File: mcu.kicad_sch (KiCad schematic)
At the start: 26 parts, among them J1 Debugger, J5 UART, J7 GPIO, SW1 BOOT, U1 STM32F103C8Tx, U2 SN65HVD230, Y1 8 Mhz 5032

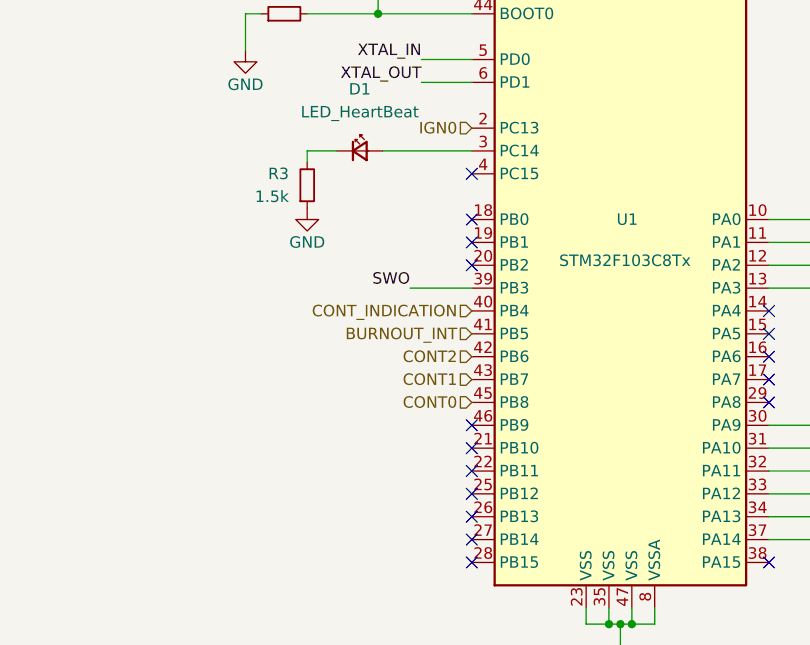
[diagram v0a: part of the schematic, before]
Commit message: Update ignition system with CDI
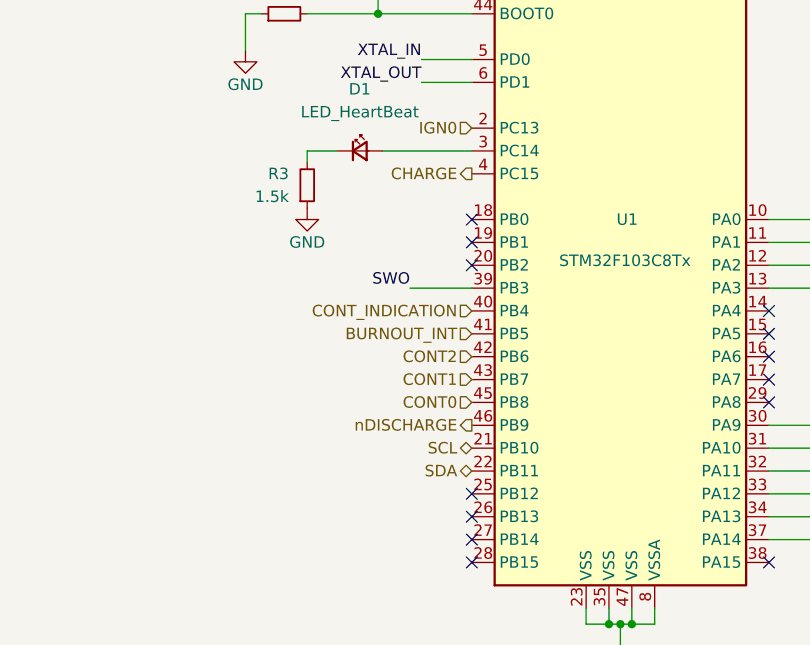
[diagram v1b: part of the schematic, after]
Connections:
- net SCL: now reaches U1.21 (PB10)
- net SDA: now reaches U1.22 (PB11)
- net CHARGE: now reaches U1.4 (PC15)
- net nDISCHARGE: now reaches U1.46 (PB9)
- no-connect marks 20 -> 16
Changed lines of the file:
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@@
   (junction (at 236.22 30.226) (diameter 0.9144) (color 0 0 0 0))
   (junction (at 236.22 38.862) (diameter 0.9144) (color 0 0 0 0))
-  (no_connect (at 74.676 97.028))
   (no_connect (at 74.676 102.108))
   (no_connect (at 74.676 104.648))
   (no_connect (at 74.676 107.188))
-  (no_connect (at 74.676 124.968))
-  (no_connect (at 74.676 127.508))
-  (no_connect (at 74.676 130.048))
   (no_connect (at 74.676 132.588))
   (no_connect (at 74.676 135.128))
@@
     (effects (font (size 1.27 1.27)) (justify right))
   )
+  (hierarchical_label "CHARGE" (shape output) (at 74.676 97.028 180)
+    (effects (font (size 1.27 1.27)) (justify right))
+  )
   (hierarchical_label "CONT_INDICATION" (shape input) (at 74.676 112.268 180)
     (effects (font (size 1.27 1.27)) (justify right))
@@
     (effects (font (size 1.27 1.27)) (justify right))
   )
+  (hierarchical_label "nDISCHARGE" (shape output) (at 74.676 124.968 180)
+    (effects (font (size 1.27 1.27)) (justify right))
+  )
+  (hierarchical_label "SCL" (shape bidirectional) (at 74.676 127.508 180)
+    (effects (font (size 1.27 1.27)) (justify right))
+  )
+  (hierarchical_label "SDA" (shape bidirectional) (at 74.676 130.048 180)
+    (effects (font (size 1.27 1.27)) (justify right))
+  )

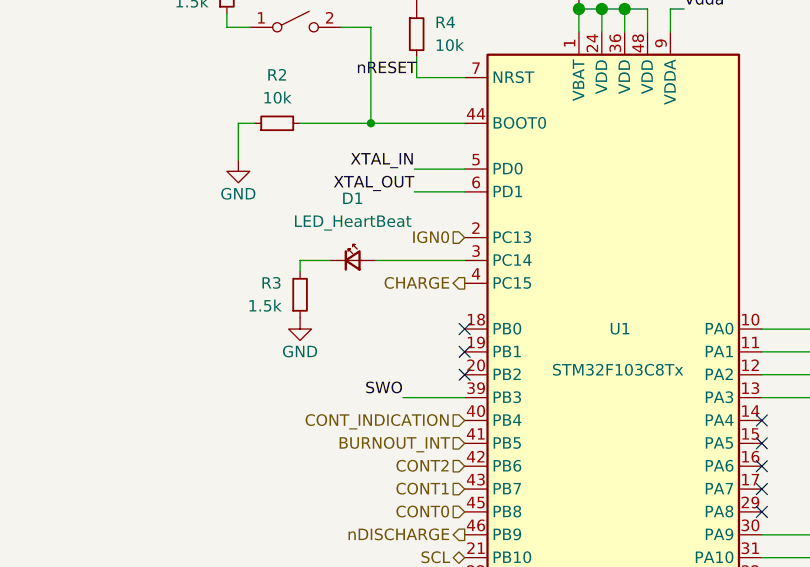
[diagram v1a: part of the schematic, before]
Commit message: #4 add pchannel for charge and nchannel for ignition
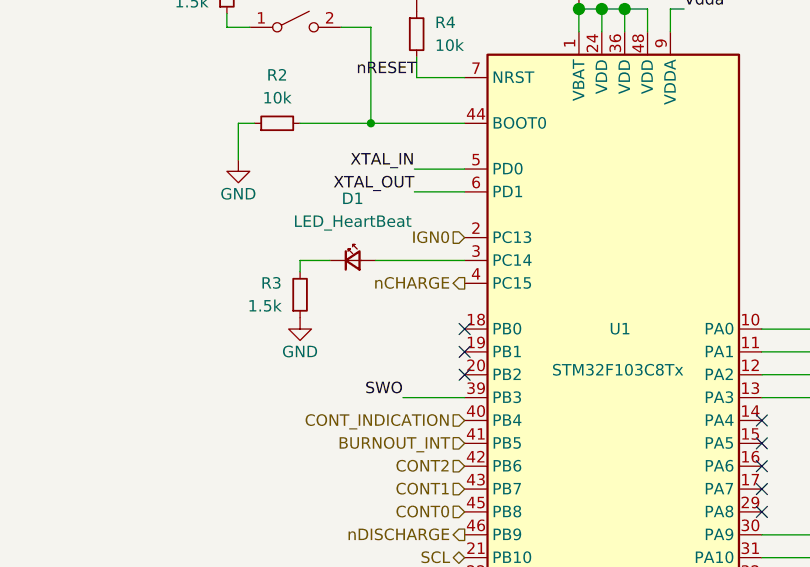
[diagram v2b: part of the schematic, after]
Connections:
- net CHARGE renamed nCHARGE
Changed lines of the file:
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@@
     (effects (font (size 1.27 1.27)) (justify right))
   )
-  (hierarchical_label "CHARGE" (shape output) (at 74.676 97.028 180)
+  (hierarchical_label "nCHARGE" (shape output) (at 74.676 97.028 180)
     (effects (font (size 1.27 1.27)) (justify right))
   )

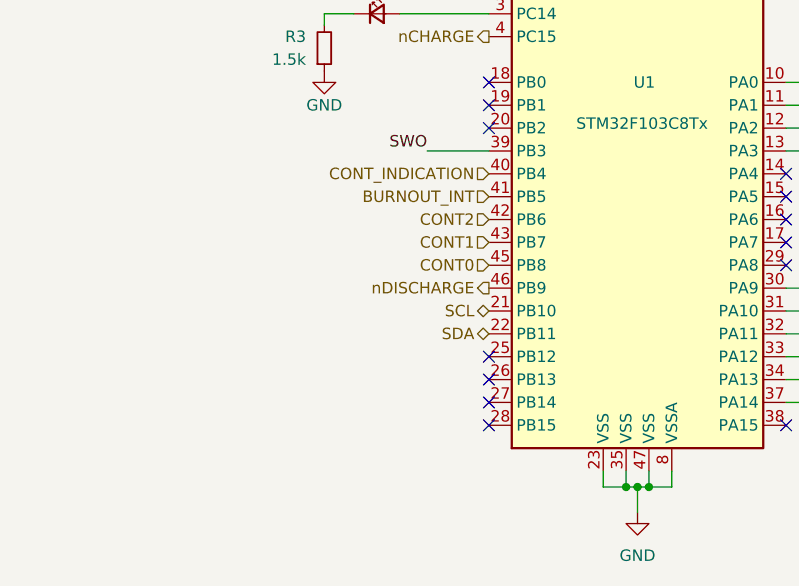
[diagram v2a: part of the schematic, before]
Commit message: #1 New pyro channel introduced in schematic
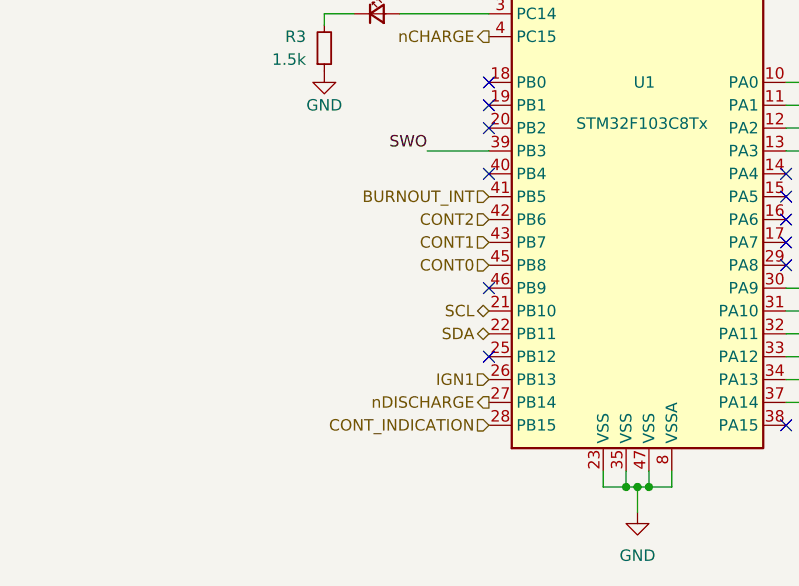
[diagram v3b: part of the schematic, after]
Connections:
- net CONT_INDICATION: now also U1.28 (PB15); no longer U1.40 (PB4)
- net nDISCHARGE: now also U1.27 (PB14); no longer U1.46 (PB9)
- net IGN1: now reaches U1.26 (PB13)
- no-connect marks 16 -> 15
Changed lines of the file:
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@@
   (no_connect (at 74.676 104.648))
   (no_connect (at 74.676 107.188))
+  (no_connect (at 74.676 112.268))
+  (no_connect (at 74.676 124.968))
   (no_connect (at 74.676 132.588))
-  (no_connect (at 74.676 135.128))
-  (no_connect (at 74.676 137.668))
-  (no_connect (at 74.676 140.208))
   (no_connect (at 107.696 112.268))
   (no_connect (at 107.696 114.808))
@@
     (effects (font (size 1.27 1.27)) (justify right))
   )
-  (hierarchical_label "CONT_INDICATION" (shape input) (at 74.676 112.268 180)
-    (effects (font (size 1.27 1.27)) (justify right))
-  )
   (hierarchical_label "BURNOUT_INT" (shape input) (at 74.676 114.808 180)
     (effects (font (size 1.27 1.27)) (justify right))
@@
     (effects (font (size 1.27 1.27)) (justify right))
   )
-  (hierarchical_label "nDISCHARGE" (shape output) (at 74.676 124.968 180)
-    (effects (font (size 1.27 1.27)) (justify right))
-  )
   (hierarchical_label "SCL" (shape bidirectional) (at 74.676 127.508 180)
     (effects (font (size 1.27 1.27)) (justify right))
@@
     (effects (font (size 1.27 1.27)) (justify right))
   )
+  (hierarchical_label "IGN1" (shape input) (at 74.676 135.128 180)
+    (effects (font (size 1.27 1.27)) (justify right))
+  )
+  (hierarchical_label "nDISCHARGE" (shape output) (at 74.676 137.668 180)
+    (effects (font (size 1.27 1.27)) (justify right))
+  )
+  (hierarchical_label "CONT_INDICATION" (shape input) (at 74.676 140.208 180)
+    (effects (font (size 1.27 1.27)) (justify right))
+  )

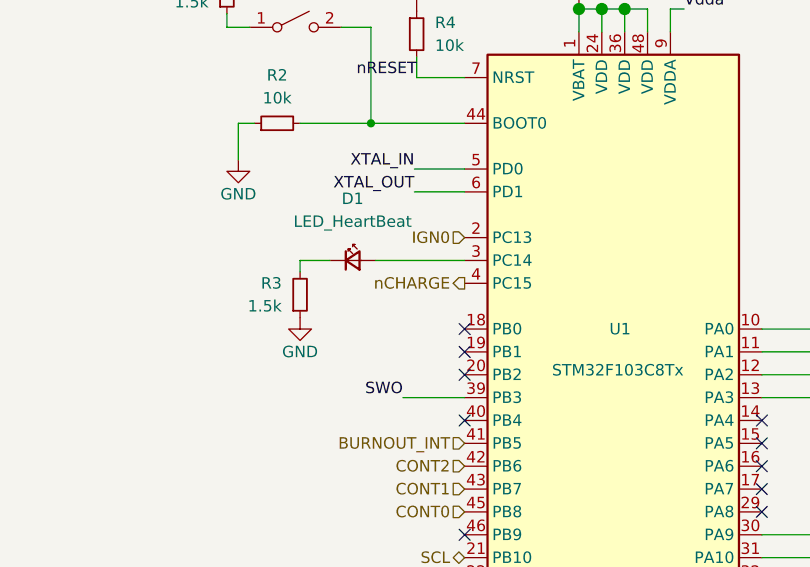
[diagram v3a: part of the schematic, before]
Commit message: Apply schematic updates to PCB
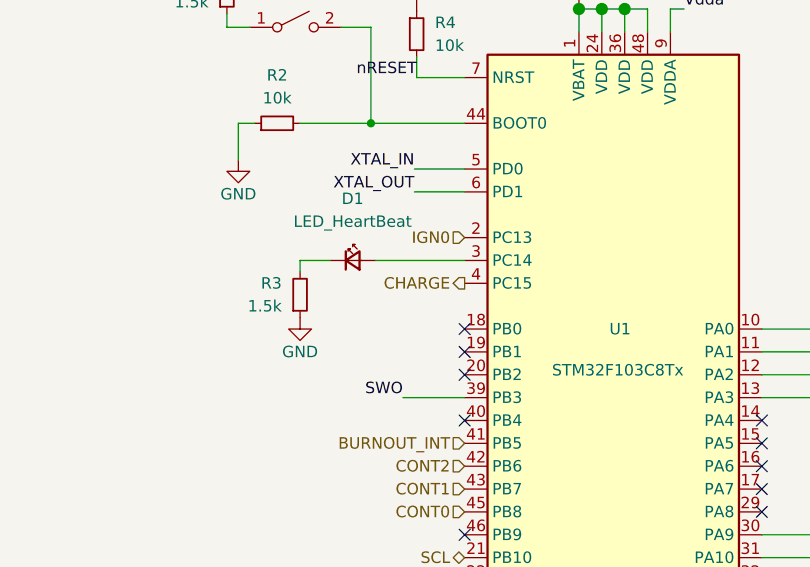
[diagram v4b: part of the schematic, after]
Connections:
- net nCHARGE renamed CHARGE
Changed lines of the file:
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@@
     (effects (font (size 1.27 1.27)) (justify right))
   )
-  (hierarchical_label "nCHARGE" (shape output) (at 74.676 97.028 180)
+  (hierarchical_label "CHARGE" (shape output) (at 74.676 97.028 180)
     (effects (font (size 1.27 1.27)) (justify right))
   )

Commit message: Bump to Rev.3
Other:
- company: (none) -> Badger
- title: (none) -> Badger-Pike: Engine Control Module
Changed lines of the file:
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@@
 (kicad_sch (version 20210621) (generator eeschema)
   (paper "A4")
+  (title_block
+    (title "Badger-Pike: Engine Control Module")
+    (date "2021-09-01")
+    (rev "Rev. 3")
+    (company "Badger")
+  )
   (junction (at 32.258 39.624) (diameter 1.36) (color 0 0 0 0))
   (junction (at 41.402 39.624) (diameter 1.36) (color 0 0 0 0))

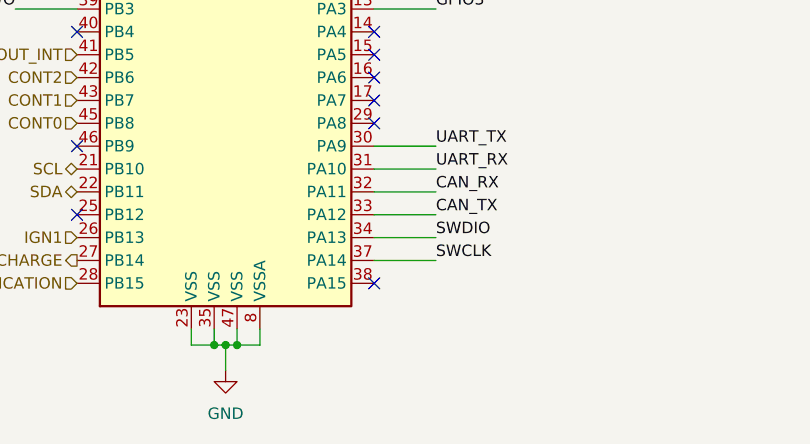
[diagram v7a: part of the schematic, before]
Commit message: #1 Make connections for IGN2
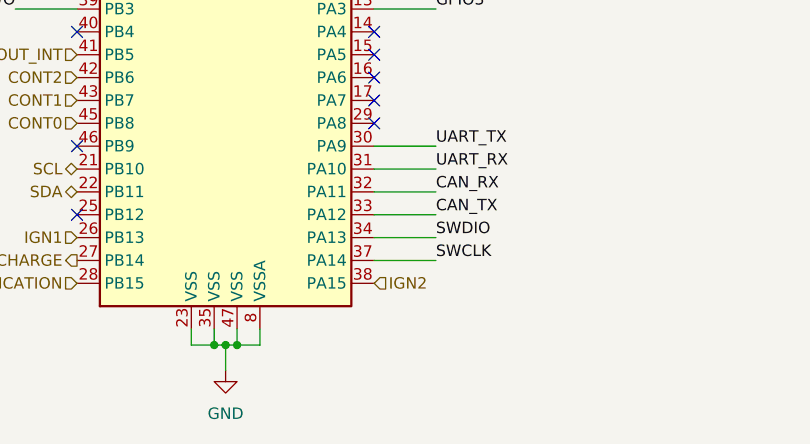
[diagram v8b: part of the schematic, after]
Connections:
- net IGN2: now reaches U1.38 (PA15)
- no-connect marks 15 -> 14
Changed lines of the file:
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@@
   (no_connect (at 107.696 119.888))
   (no_connect (at 107.696 122.428))
-  (no_connect (at 107.696 140.208))
   (no_connect (at 162.56 40.894))
   (no_connect (at 175.26 40.894))
@@
     (effects (font (size 1.27 1.27)) (justify right))
   )
+  (hierarchical_label "IGN2" (shape input) (at 107.696 140.208 0)
+    (effects (font (size 1.27 1.27)) (justify left))
+  )
   (hierarchical_label "CAN+" (shape bidirectional) (at 251.968 30.226 0)
